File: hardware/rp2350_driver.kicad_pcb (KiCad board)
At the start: 6 copper layers, 76 x 46.4 mm, 319 parts, among them J1 XT30, J10 Power Output, J11 CAN2 PLUG, J12 Conn_01x06, J2 XT30, J3 USB_C_Receptacle_USB2.0, J4 SM03B-SRSS-TB, J5 Estop Conn, J6 SM03B-SRSS-TB, J7 Conn_01x03, J8 Conn_01x03, J9 XT30, Q1 Q_PNP_BEC, Q2 Q_PNP_BEC, Q3 Q_PNP_BEC, Q4 Q_PNP_BEC, Q5 Q_NMOS_GDS, Q6 Q_NMOS_GDS, SW1 Button, SW2 Button, U1 EG3113, U10 INA240A1D, U101 FUSB302BMPX, U11 USBLC6-2P6, U12 EG3113, U13 TS5A3159DCK, U14 TS5A3159DCK, U15 TS5A3159DCK, U16 CA-IS3052CG, U17 TS5A3159DCK, U18 SIT3088ETK, U19 SIT3088ETK, U20 SIT3088ETK, U21 SIT3088ETK, U22 TS5A3159DCK, U23 TS5A3159DCK, U24 TS5A3159DCK, U25 TS5A3159DCK, U26 TS5A3159DCK, U27 TS5A3159DCK, U28 XL7005A, U29 LM74700, U3 W25Q16JV, U30 TS5A3159DCK, U31 TS5A3159DCK, U32 TS5A3159DCK, U33 TS5A3159DCK, U4 SPX3819M5-L-3-3, U5 INA240A1D, U6 EG3113, U7 EG3113, U8 RP2350_80QFN, U9 INA240A1D, Y1 ABM8-272-T3

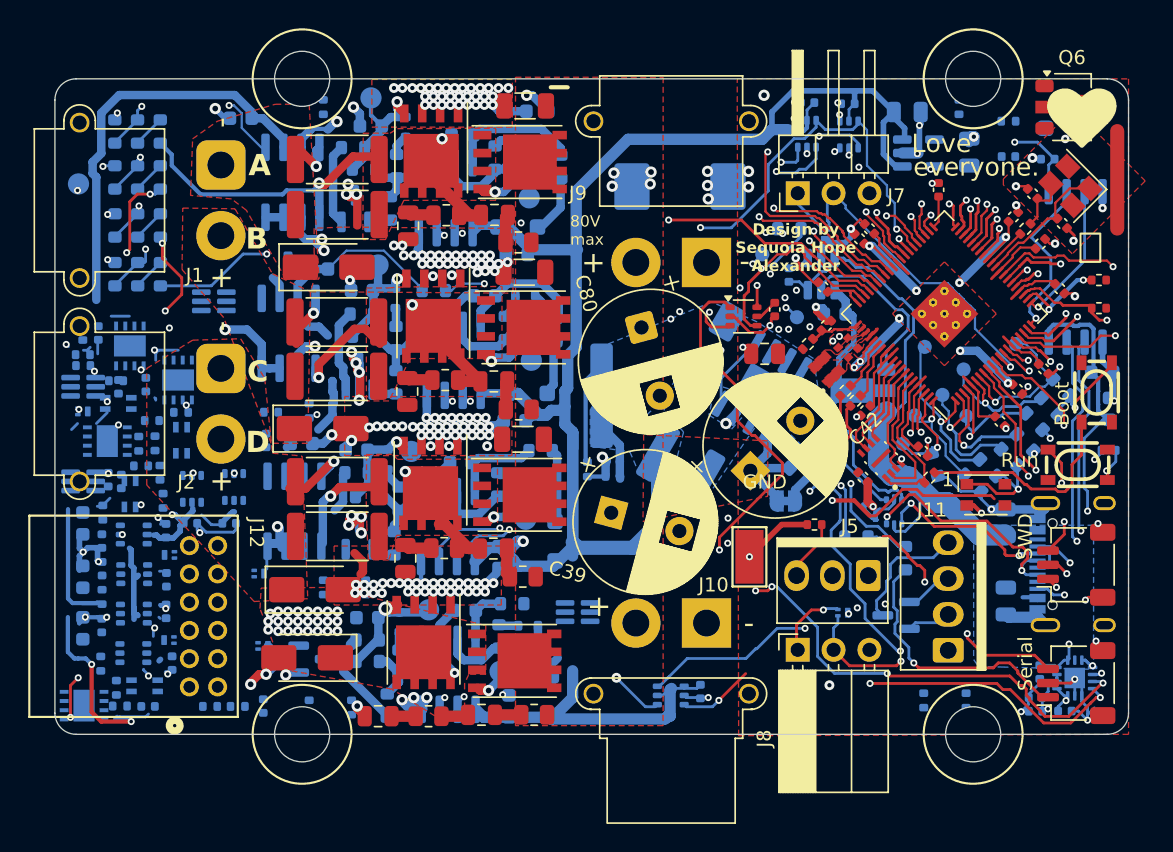
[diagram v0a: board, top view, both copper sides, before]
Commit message: board prep for morph gate: 1mm encoder-edge extension, true-shape courtyards, J3 NPTH keepouts; prerip project file so kicad-cli DRC uses real rules
Co-Authored-By: Claude Fable 5 <noreply@anthropic.com>
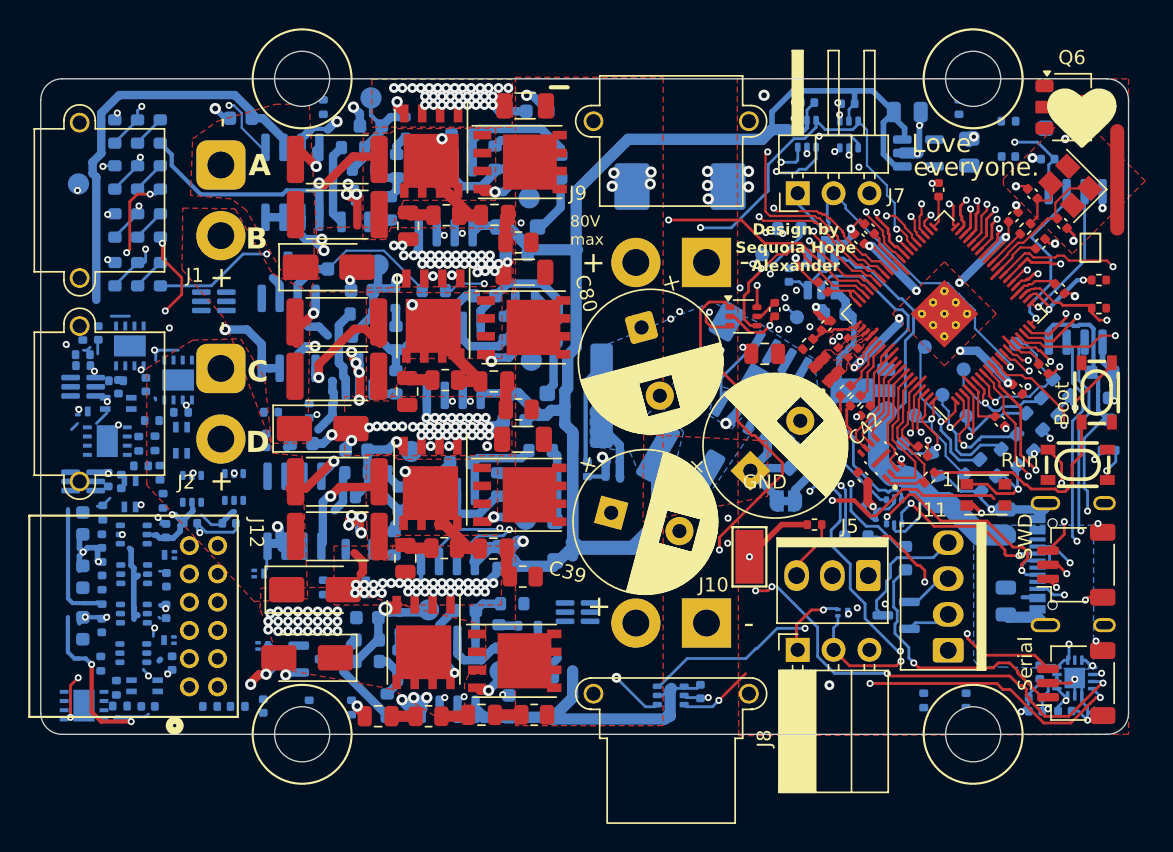
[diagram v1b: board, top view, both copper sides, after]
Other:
- board size 76 x 46.4 mm -> 77 x 46.4 mm

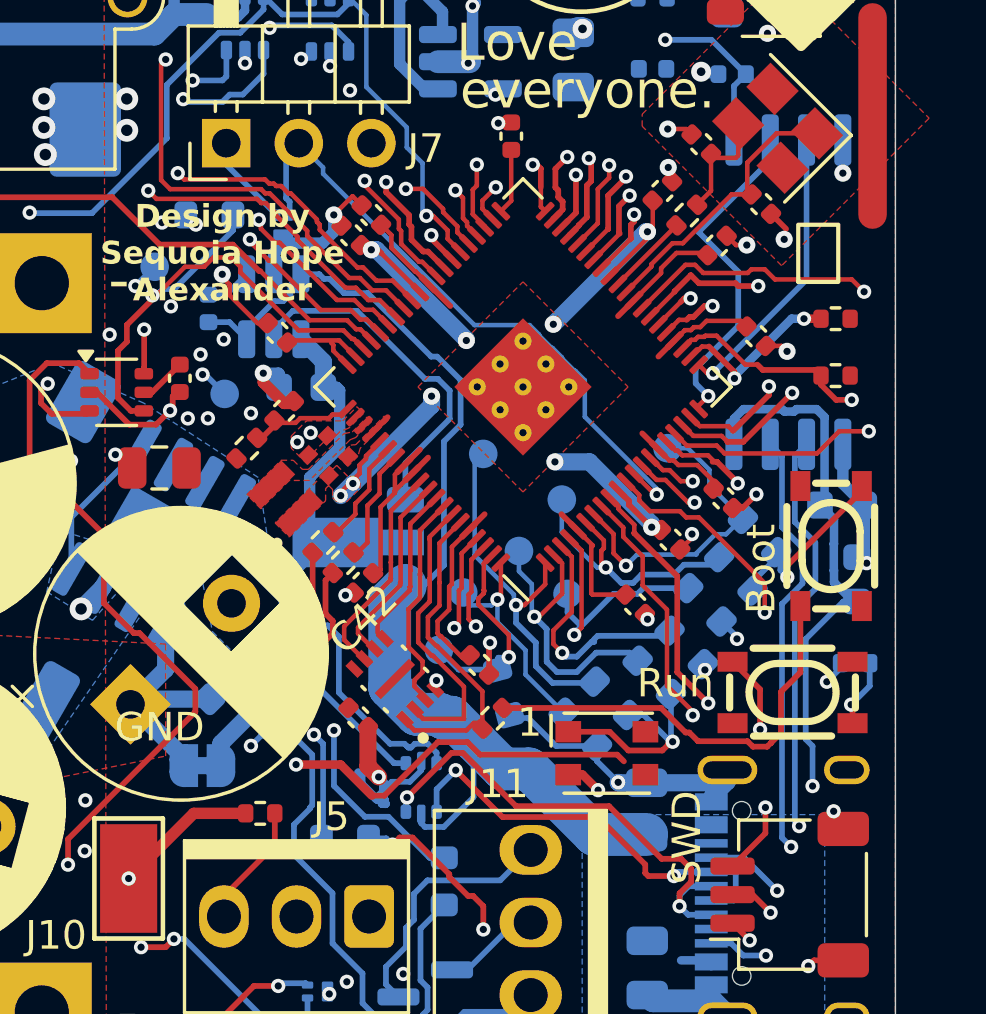
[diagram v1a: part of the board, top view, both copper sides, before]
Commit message: rev-B PCB: sync F-27/F-39 to the schematic + placement (routing still due)
The schematic side of F-27/F-39 landed in 7058e41 with the PCB deliberately
left alone, on the read that both new footprints collided with five real
neighbours each and needed a placement session. That read was wrong: it counted
courtyards on the OPPOSITE copper side. U29 and Q5 are B.Cu parts, and most of
what looked like a collision (C45, C21, C24, R32, L2, C18, C17, C30, R50, R51)
is on F.Cu, where a courtyard cannot clash. Same-side, the job is small.

kicad-cli has no "update PCB from schematic" and pcbnew's SWIG bindings expose
no BOARD_NETLIST_UPDATER, so the sync is explicit, in tools/revb/:

  check_sync.py  exports the schematic netlist and diffs components, footprint
                 assignments and per-pad nets against the board. It classifies
                 the shipped board's pre-existing noise (27 footprints with no
                 library nickname, stale symbol-name values, unconnected-pad
                 naming, board-only thermal pads) instead of drowning in it.
                 This is the acceptance test, and it now says IN SYNC.
  scan_place.py  pose search. Drops the real footprint on the board at every
                 0.25 mm / 90 deg pose and asks KiCad for courtyards and pad
                 geometry. Hard constraints (same-side courtyard of a real
                 part, any other-net pad, board edge) must be zero; other-net
                 track segments crossed are the cost, since each is copper
                 someone must route again.
  sync_pcb.py    applies the delta, then verifies and refills before writing.

Placement chosen:

  U29  LTC4359 MSOP-8 at (167.745, 95.825) rot 0 - 1.00 mm east of the old
       SOT-23-6 centroid, rotated to horizontal into the space C79 vacated.
       Zero courtyard conflicts, zero test-point moves, zero extra copper.
  Q5   PowerPAK SO-8 at (170.400, 103.325) rot 180 - source east toward J3,
       drain west toward JP1, 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
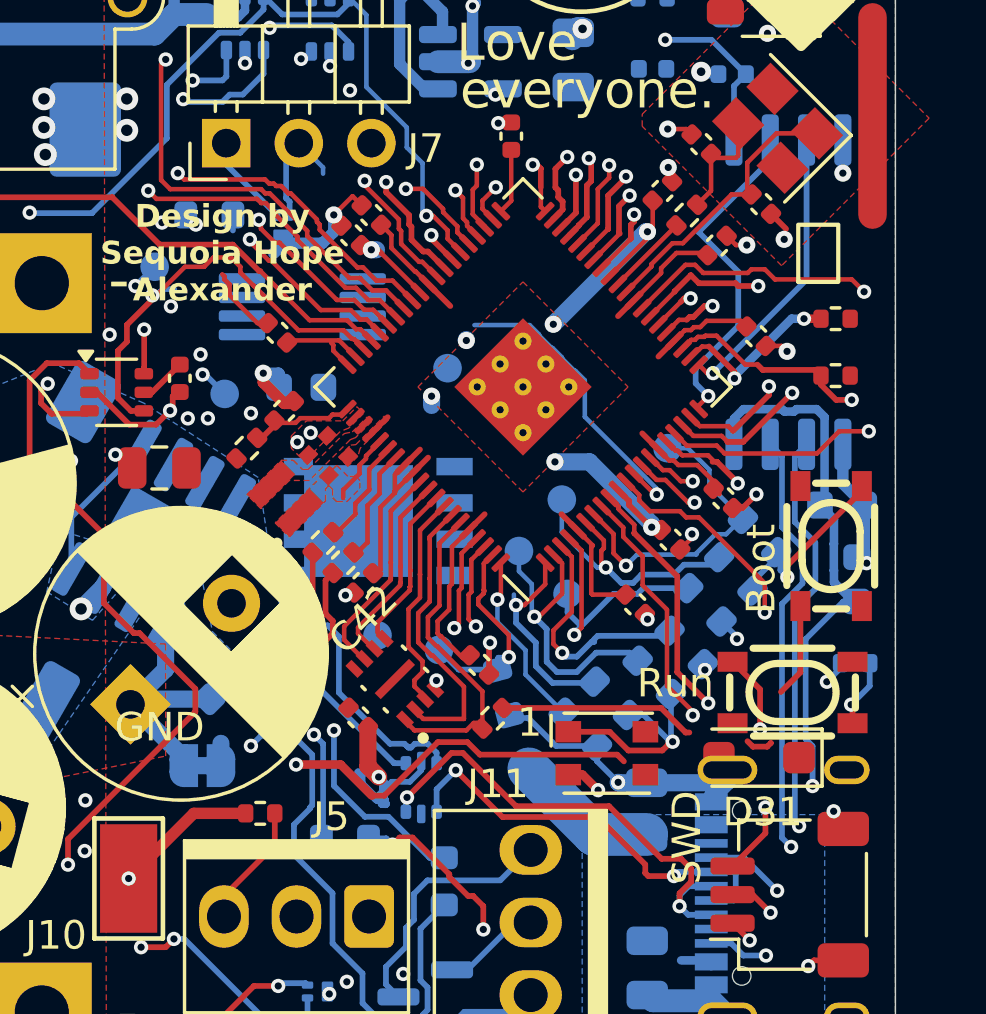
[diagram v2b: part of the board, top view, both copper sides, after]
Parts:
- removed C79: 100n, Capacitor_SMD:C_0402_1005Metric
- added D31: SMF24A, Diode_SMD:D_SOD-123F, F.Cu at (183.7, 111.6)
- Q5: value Q_NMOS_GDS -> E100N4P0HL1; footprint Package_TO_SOT_SMD:SOT-89-3 -> parts:PowerPAK_SO-8_123
- U29: value LM74700 -> LTC4359CMS8; footprint Package_TO_SOT_SMD:SOT-23-6 -> Package_SO:MSOP-8_3x3mm_P0.65mm
- moved TP15 3.35 mm to (170.4, 107.3)
- moved TP17 3.25 mm to (172.8, 98.0)
- moved Q5 1.25 mm to (170.4, 103.3)
- moved U29 1.00 mm to (167.7, 95.8), turned to 0 degrees
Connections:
- Q5 pad 1: Net-(Q5-G) -> VBUS
- Q5 pad 2: Net-(JP1-A) -> Net-(Q5-G)
- Q5 pad 3: VBUS -> Net-(JP1-A)
- U11 pad 5: VBUS -> +3V3
- U29 pad 1: Net-(U29-VCAP) -> Net-(Q5-G)
- U29 pad 2: GND -> VBUS
- U29 pad 3: VBUS -> unconnected-(U29-NC-Pad3)
- U29 pad 4: Net-(JP1-A) -> VBUS
- U29 pad 5: Net-(Q5-G) -> VBUS
- U29 pad 6: VBUS -> GND
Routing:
- net VBUS: track 41.1 -> 6.21 mm
- net Net-(JP1-A): track 23.8 -> 0.78 mm
- net Net-(Q5-G): track 12.4 -> 0.00 mm
- net +1V1: track 29.2 -> 20.3 mm, vias 9 -> 7
- net /RXI_INTERBOARD_1: track 22.5 -> 15.0 mm
- net B_PWM_H: track 49.4 -> 43.8 mm
- net A_PWM_L\: track 48.7 -> 44.0 mm
- net /~{USB_BOOT}: track 15.2 -> 11.1 mm
- net /TH1_SENSE: track 18.9 -> 16.0 mm
- net Net-(U29-VCAP): track 1.63 -> 0.00 mm
- net GND: track 198.2 -> 197.5 mm, vias 231 -> 230
- net /ENC_C_SW: vias 3 -> 2

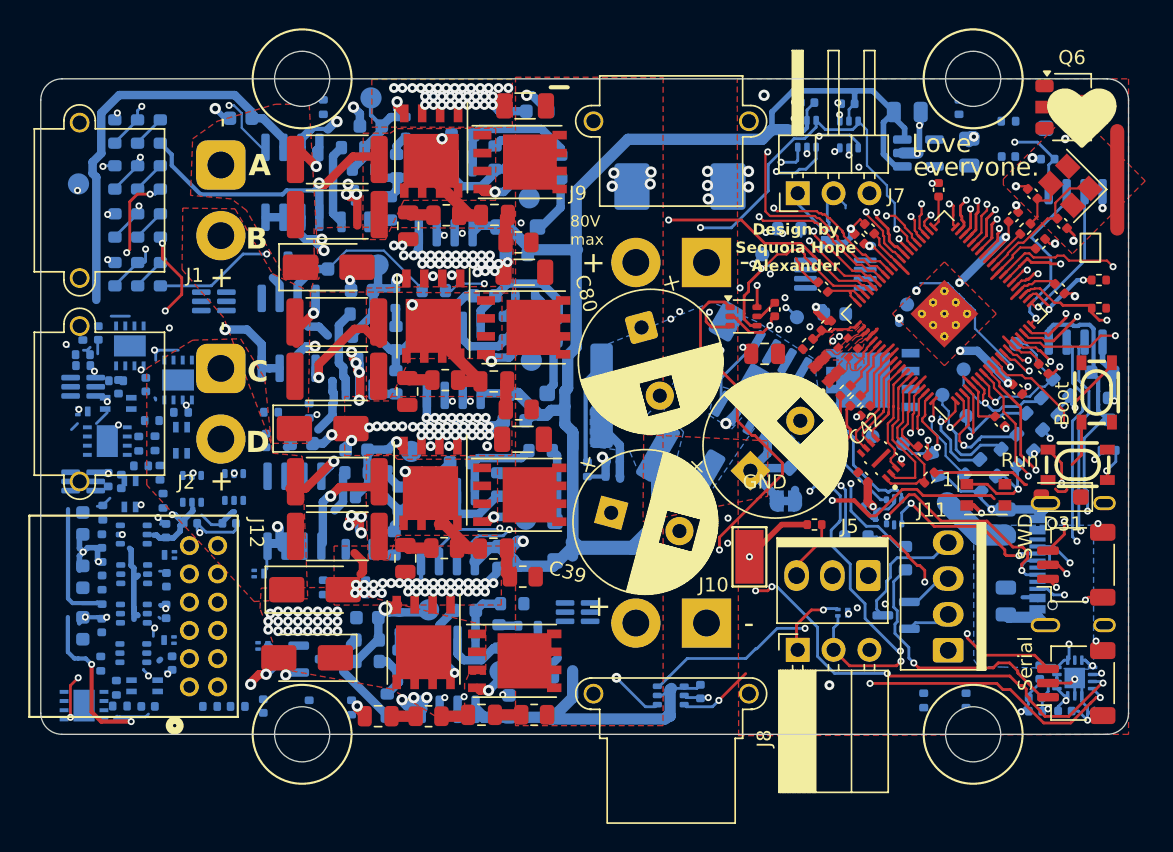
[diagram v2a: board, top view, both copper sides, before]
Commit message: rev-B: module-stretch verdict (F-44), rev-B parts re-placed + F-19 landed, Q6 SOT-23 (F-45), corner routed 238->54 airwires
Module stretch (review/modules.html, hardware/tools/modules/): the board carved
into 14 parent modules / 47 rigid leaves + 16 pinned interfaces; exact-polygon
slack probe, sequential-LP stretch, connectivity-owned copper warp, kicad DRC
referee. Verdict F-44: no module-level slack -- the DRC-neutral stretch is 5
loose parts (applied, signature-identical DRC); every dense-module move sheds
DRC violations through rule-pitch seam copper.

Placement: pose scanner on real KiCad geometry re-placed the 17 provisional
rev-B parts (U30-U33, C110-C113, R97-R100, R101/103/104/105/108), landed the
F-19 CAN parts (R114/JP2 by J11, C115 on the front between J11/J6, R115), and
swapped Q6 to the schematic's SOT-23 (F-45; check_sync known-exceptions now
empty). Corner cleanup removed the stray copper under the relaxed parts.

Routing: Freerouting with all copper locked hangs on this board; in-house
grid router (router.py) + GND plane stitching closed 197 of 251 connections.
Board: DRC 167 -> 4 (four cosmetic mask bridges), airwires 238 -> 54,
check_sync IN SYNC. F-25 stays open: the 54 left are named placement fixes.

Also lands the earlier uncommitted rev-B work on this branch: F-19 schematic
(add_f19_can_termination.py), F-43 0603->0402 shrink (shrink_0402.py), and
the F-19/F-42/F-43 register rows.

Co-Authored-By: Claude Fable 5 <noreply@anthropic.com>
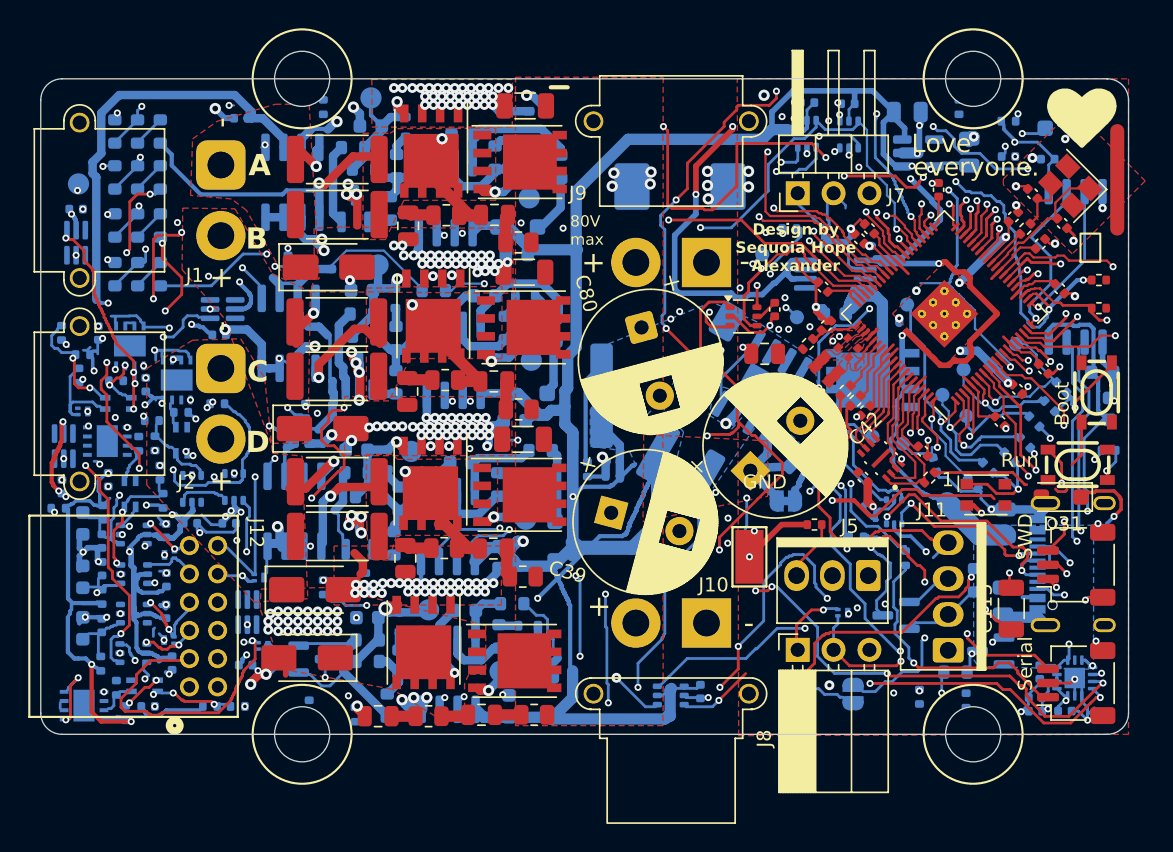
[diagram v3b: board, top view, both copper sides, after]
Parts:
- added C115: 1n 2kV, Capacitor_SMD:C_1206_3216Metric, F.Cu at (180.2, 119.5)
- added JP2: Jumper_2_Open, Jumper:SolderJumper-2_P1.3mm_Open_RoundedPad1.0x1.5mm, B.Cu at (169.0, 125.5)
- added R114: 120R, Resistor_SMD:R_0603_1608Metric, B.Cu at (177.6, 117.5)
- added R115: 100R, Resistor_SMD:R_0603_1608Metric, B.Cu at (176.2, 124.0)
- C16, C19, C29, C40: footprint Capacitor_SMD:C_0603_1608Metric -> Capacitor_SMD:C_0402_1005Metric
- Q6: footprint SOT-89-3 -> Package_TO_SOT_SMD:SOT-23; moved to B.Cu
- R1, R2, R21, R22, R35, R36, R49, R53, R54, R65, R66: footprint Resistor_SMD:R_0603_1608Metric -> Resistor_SMD:R_0402_1005Metric
- moved Q6 38.9 mm to (178.8, 122.5), turned to 180 degrees
- moved U31 23.4 mm to (126.1, 119.8), turned to 90 degrees
- moved C113 12.9 mm to (114.0, 91.2), turned to 0 degrees
- moved U33 10.2 mm to (114.0, 93.6), turned to 90 degrees
- moved C112 8.18 mm to (124.1, 100.1), turned to 0 degrees
- moved R97 6.57 mm to (112.8, 112.4), turned to 180 degrees
- moved C110 4.22 mm to (113.0, 110.9)
- moved R99 3.85 mm to (124.0, 105.0)
- moved C111 3.16 mm to (126.0, 123.5), turned to 0 degrees
- moved U30 2.85 mm to (113.1, 108.0), turned to 90 degrees
- moved R103 2.85 mm to (143.8, 107.8), turned to 180 degrees
- moved R91 1.51 mm to (113.0, 100.0), turned to 90 degrees
- moved U32 0.83 mm to (124.4, 98.3)
- moved R100 0.76 mm to (114.2, 103.0), turned to 90 degrees
- moved R98 0.64 mm to (117.5, 126.9), turned to 90 degrees
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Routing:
- net Vdrive: track 224.1 -> 373.3 mm, vias 3 -> 19
- net /I2C_SDA: track 89.2 -> 212.8 mm, vias 4 -> 12
- net /H2_SW: track 69.5 -> 188.4 mm, vias 1 -> 9
- net /E-STOP: track 23.0 -> 141.9 mm, vias 1 -> 16
- net VBUS: track 6.21 -> 98.6 mm, vias 0 -> 6
- net /ENC_A_SW: track 70.5 -> 152.4 mm, vias 1 -> 5
- net /HALL1: track 80.2 -> 143.1 mm, vias 1 -> 4
- net /HALL2: track 84.9 -> 143.6 mm, vias 1 -> 4
- net /ENC_C_SW: track 58.9 -> 112.2 mm, vias 2 -> 10
- net /MOT_TH: track 50.3 -> 95.9 mm, vias 1 -> 3
- net +3V3: track 204.2 -> 248.2 mm, vias 15 -> 26
- net /H1_SW: track 70.4 -> 112.0 mm, vias 2 -> 5
- net /TH_SW_1: track 22.2 -> 61.8 mm, vias 2 -> 4
- net /ENC_C_P: track 0.00 -> 31.6 mm, vias 0 -> 3
- net GND_ISO: track 30.3 -> 56.7 mm, vias 1 -> 3
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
